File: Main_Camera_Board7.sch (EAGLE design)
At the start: 8 parts

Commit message: made a few changes to camera board
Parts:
- removed LIGHT, LIGHT1: (no value), con-lsta:FE05-1
- added JP1, JP2: (no value), pinhead:PINHD-1X2
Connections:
- net +3.3V: no longer LIGHT.5, LIGHT1.5
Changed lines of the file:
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@@
 <?xml version="1.0" encoding="utf-8"?>
 <!DOCTYPE eagle SYSTEM "eagle.dtd">
-<eagle version="7.6.0">
+<eagle version="7.7.0">
 <drawing>
 <settings>
@@
 <layers>
 <layer number="1" name="Top" color="4" fill="1" visible="no" active="no"/>
+<layer number="2" name="Route2" color="1" fill="3" visible="no" active="no"/>
+<layer number="3" name="Route3" color="4" fill="3" visible="no" active="no"/>
+<layer number="14" name="Route14" color="1" fill="6" visible="no" active="no"/>
+<layer number="15" name="Route15" color="4" fill="6" visible="no" active="no"/>
 <layer number="16" name="Bottom" color="1" fill="1" visible="no" active="no"/>
 <layer number="17" name="Pads" color="2" fill="1" visible="no" active="no"/>
@@
 <part name="FRAME1" library="frames" deviceset="DINA3_L" device=""/>
 <part name="SERVO" library="con-lsta" deviceset="FE05-1" device=""/>
-<part name="LIGHT" library="con-lsta" deviceset="FE05-1" device=""/>
-<part name="LIGHT1" library="con-lsta" deviceset="FE05-1" device=""/>
 <part name="U$1" library="camera" deviceset="ELP-USBFHD01M-L21" device=""/>
 <part name="U$2" library="camera" deviceset="LED" device=""/>
@@
 <part name="U$4" library="camera" deviceset="T21" device=""/>
 <part name="U$5" library="camera" deviceset="T21" device=""/>
+<part name="JP1" library="pinhead" deviceset="PINHD-1X2" device=""/>
+<part name="JP2" library="pinhead" deviceset="PINHD-1X2" device=""/>
 </parts>
 <sheets>
@@
 <instance part="FRAME1" gate="G$2" x="287.02" y="0"/>
 <instance part="SERVO" gate="G$1" x="124.46" y="154.94" rot="R270"/>
-<instance part="LIGHT" gate="G$1" x="175.26" y="154.94"/>
-<instance part="LIGHT1" gate="G$1" x="182.88" y="116.84"/>
 <instance part="U$1" gate="G$1" x="119.38" y="104.14" rot="R90"/>
 <instance part="U$2" gate="G$1" x="83.82" y="139.7"/>
@@
 <instance part="U$4" gate="G$1" x="81.28" y="106.68" rot="R90"/>
 <instance part="U$5" gate="G$1" x="81.28" y="91.44" rot="R90"/>
+<instance part="JP1" gate="G$1" x="152.4" y="160.02" rot="R180"/>
+<instance part="JP2" gate="G$1" x="152.4" y="134.62" rot="R180"/>
 </instances>
 <busses>
@@
 <net name="+3.3V" class="0">
 <segment>
-<pinref part="LIGHT" gate="G$1" pin="5"/>
-<wire x1="182.88" y1="160.02" x2="205.74" y2="160.02" width="0.1524" layer="91"/>
-<label x="198.12" y="160.02" size="1.778" layer="95"/>
-</segment>
-<segment>
-<pinref part="LIGHT1" gate="G$1" pin="5"/>
-<wire x1="190.5" y1="121.92" x2="205.74" y2="121.92" width="0.1524" layer="91"/>
-<label x="200.66" y="121.92" size="1.778" layer="95"/>
-</segment>
-<segment>
 <pinref part="U$5" gate="G$1" pin="P$3"/>

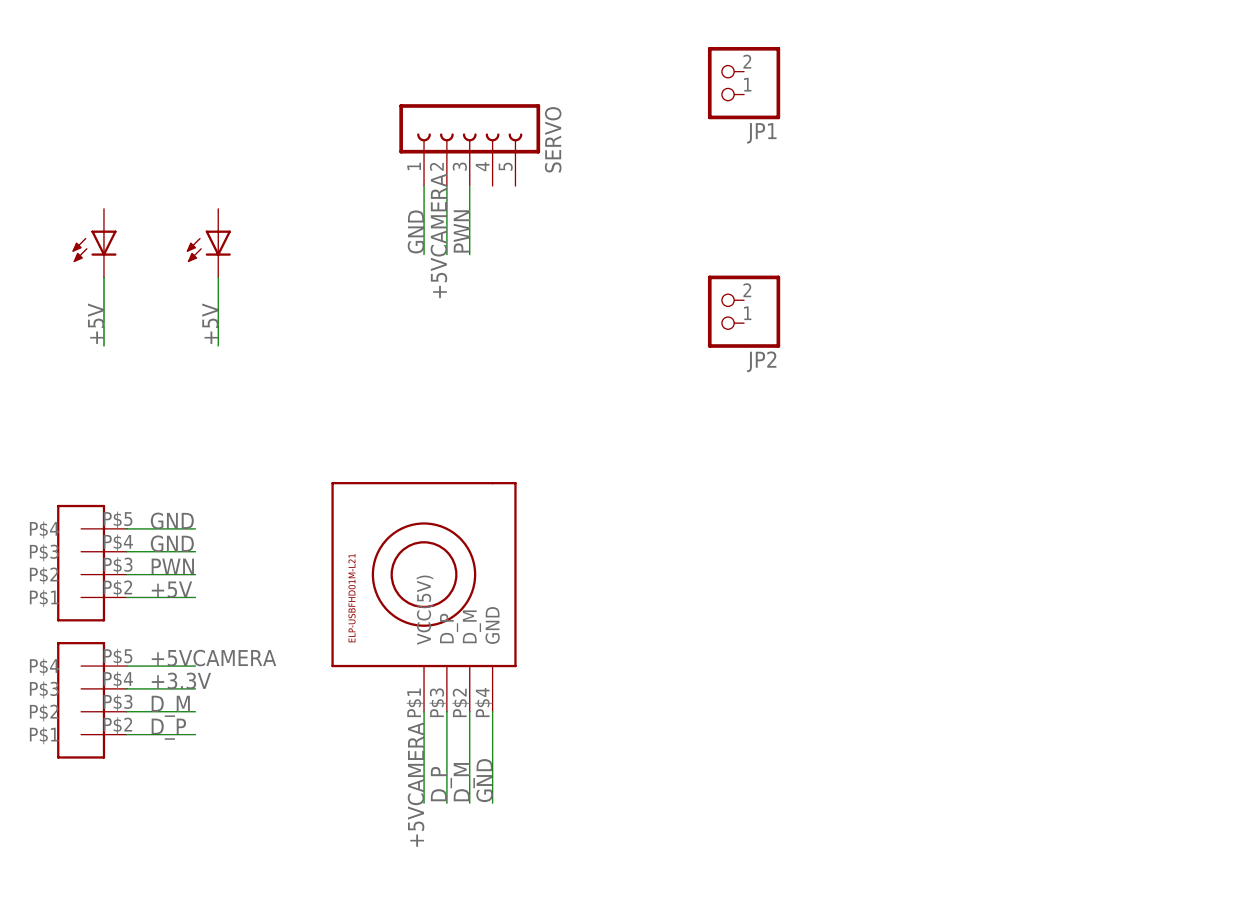
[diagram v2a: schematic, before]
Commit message: Fixed schematic errors
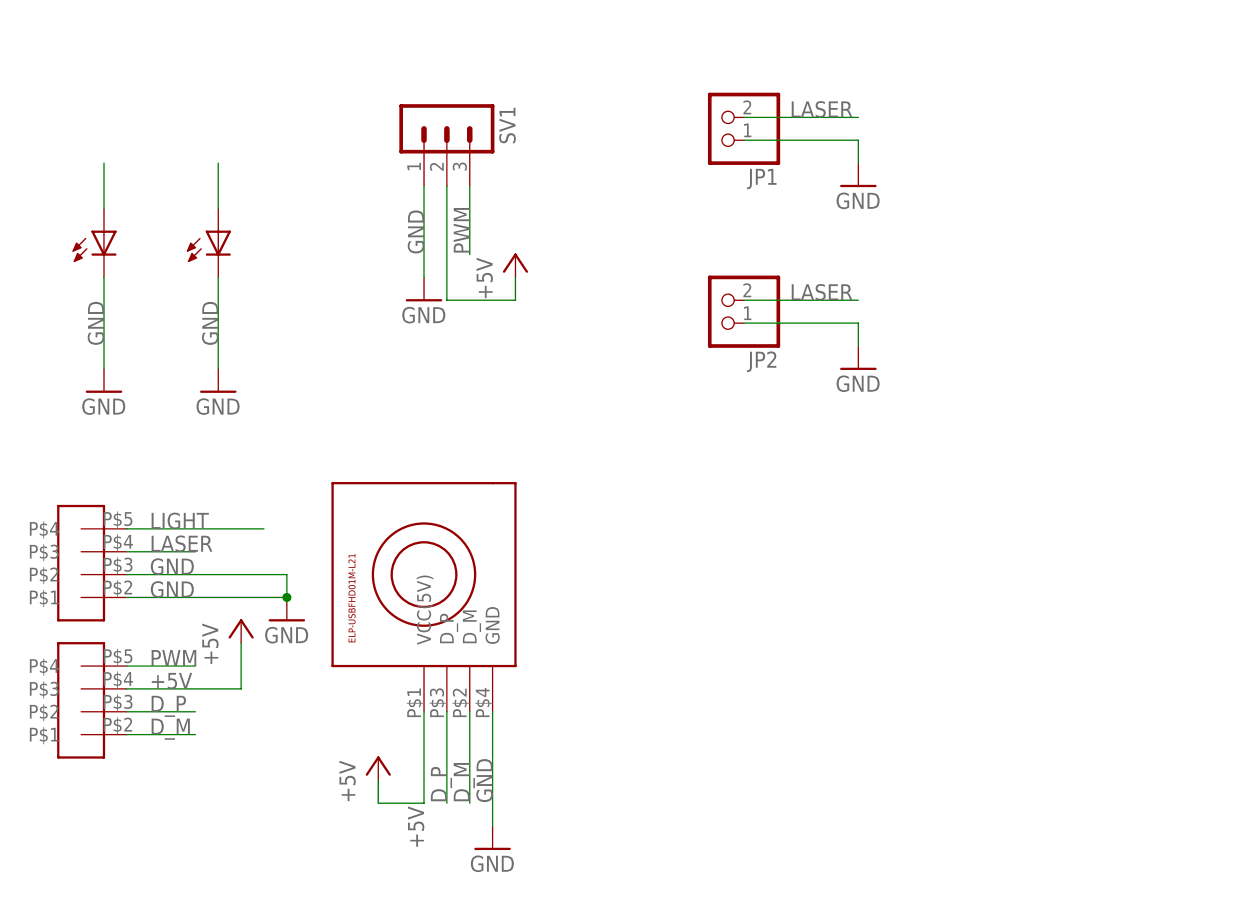
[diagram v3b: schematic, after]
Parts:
- removed SERVO: (no value), con-lsta:FE05-1
- added SV1: (no value), con-lstb:MA03-1
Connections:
- removed net +3.3V: U$5.P$3
- removed net +5VCAMERA: SERVO.2, U$1.VCC(5V), U$5.P$4
- removed net PWN: SERVO.3, U$4.P$2
- new net LASER: JP1.2, JP2.2, U$4.P$3
- new net LIGHT: U$2.ANODE, U$3.ANODE, U$4.P$4
- new net PWM: SV1.3, U$5.P$4
- net +5V: now also SV1.2, U$1.VCC(5V), U$5.P$3; no longer U$2.CATHODE, U$3.CATHODE, U$4.P$1
- net D_M: now also U$5.P$1; no longer U$5.P$2
- net D_P: now also U$5.P$2; no longer U$5.P$1
- net GND: now also JP1.1, JP2.1, SV1.1, U$2.CATHODE, U$3.CATHODE, U$4.P$1, U$4.P$2; no longer SERVO.1, U$4.P$3, U$4.P$4
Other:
- moved on the sheet: JP1
